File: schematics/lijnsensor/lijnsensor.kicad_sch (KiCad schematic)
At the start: 29 parts, among them J1 Conn_01x04_Pin, U10 AS7343xDLG, U11 AS7343xDLG, U2 TCA9548APWR, U3 TLV75718PDBV, U4 AS7343xDLG, U5 AS7343xDLG, U6 AS7343xDLG, U7 AS7343xDLG, U8 AS7343xDLG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

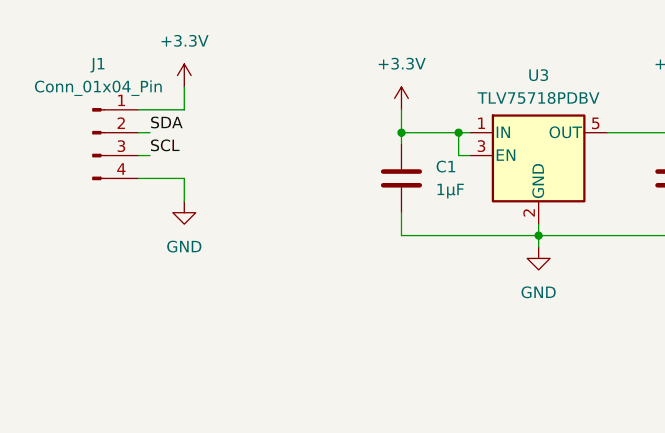
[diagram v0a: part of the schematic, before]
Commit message: ESD bescherming voor de lijnsensor
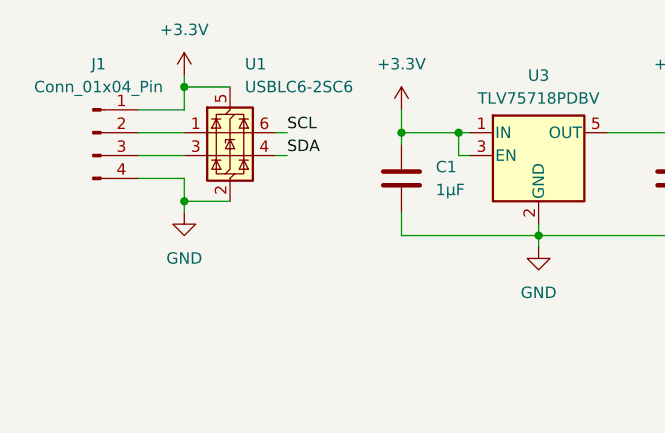
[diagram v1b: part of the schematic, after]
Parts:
- added U1: USBLC6-2SC6, Package_TO_SOT_SMD:SOT-23-6, symbol Power_Protection:USBLC6-2SC6
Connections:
- net +3.3V: now also U1.5 (VBUS)
- net GND: now also U1.2 (GND)
- net SCL: now also U1.6 (I/O1); no longer J1.3 (Pin_3)
- net SDA: now also U1.4 (I/O2); no longer J1.2 (Pin_2)
- new net: J1.2 (Pin_2), U1.1 (I/O1)
- new net: J1.3 (Pin_3), U1.3 (I/O2)
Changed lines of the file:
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@@
 	)
 	(junction
+		(at 33.02 21.59)
+		(diameter 0)
+		(color 255 0 0 1)
+	)
+	(junction
 		(at 78.74 160.02)
 		(diameter 0)
@@
 	)
 	(junction
+		(at 33.02 34.29)
+		(diameter 0)
+		(color 0 0 0 1)
+	)
+	(junction
 		(at 149.86 83.82)
 		(diameter 0)
@@
 	(wire
 		(pts
+			(xy 27.94 29.21) (xy 33.02 29.21)
+		)
+		(stroke
+			(width 0)
+			(type default)
+		)
+	)
+	(wire
+		(pts
 			(xy 147.32 151.13) (xy 147.32 154.94)
 		)
@@
 	(wire
 		(pts
+			(xy 33.02 21.59) (xy 38.1 21.59)
+		)
+		(stroke
+			(width 0)
+			(type default)
+			(color 255 0 0 1)
+		)
+	)
+	(wire
+		(pts
 			(xy 125.73 158.75) (xy 125.73 160.02)
 		)
@@
 	(wire
 		(pts
+			(xy 43.18 26.67) (xy 44.45 26.67)
+		)
+		(stroke
+			(width 0)
+			(type default)
+		)
+	)
+	(wire
+		(pts
 			(xy 72.39 36.83) (xy 72.39 38.1)
 		)
@@
 	(wire
 		(pts
-			(xy 27.94 26.67) (xy 29.21 26.67)
-		)
-		(stroke
-			(width 0)
-			(type default)
-		)
-	)
-	(wire
-		(pts
 			(xy 106.68 31.75) (xy 133.35 31.75)
 		)
@@
 	(wire
 		(pts
-			(xy 27.94 29.21) (xy 29.21 29.21)
+			(xy 114.3 147.32) (xy 100.33 147.32)
 		)
 		(stroke
@@
 	(wire
 		(pts
-			(xy 114.3 147.32) (xy 100.33 147.32)
+			(xy 100.33 144.78) (xy 113.03 144.78)
 		)
 		(stroke
@@
 	(wire
 		(pts
-			(xy 100.33 144.78) (xy 113.03 144.78)
+			(xy 125.73 72.39) (xy 125.73 73.66)
 		)
 		(stroke
@@
 	(wire
 		(pts
-			(xy 125.73 72.39) (xy 125.73 73.66)
+			(xy 109.22 170.18) (xy 100.33 170.18)
 		)
 		(stroke
@@
 	(wire
 		(pts
-			(xy 109.22 170.18) (xy 100.33 170.18)
+			(xy 33.02 34.29) (xy 33.02 35.56)
 		)
 		(stroke
 			(width 0)
 			(type default)
+			(color 0 0 0 1)
 		)
 	)
@@
 	(wire
 		(pts
+			(xy 33.02 21.59) (xy 33.02 24.13)
+		)
+		(stroke
+			(width 0)
+			(type default)
+			(color 255 0 0 1)
+		)
+	)
+	(wire
+		(pts
 			(xy 100.33 162.56) (xy 133.35 162.56)
 		)
@@
 	(wire
 		(pts
+			(xy 27.94 26.67) (xy 33.02 26.67)
+		)
+		(stroke
+			(width 0)
+			(type default)
+		)
+	)
+	(wire
+		(pts
 			(xy 125.73 95.25) (xy 115.57 95.25)
 		)
@@
 	(wire
 		(pts
+			(xy 43.18 29.21) (xy 44.45 29.21)
+		)
+		(stroke
+			(width 0)
+			(type default)
+		)
+	)
+	(wire
+		(pts
 			(xy 121.92 160.02) (xy 121.92 165.1)
 		)
@@
 	(wire
 		(pts
-			(xy 33.02 21.59) (xy 33.02 24.13)
+			(xy 33.02 20.32) (xy 33.02 21.59)
 		)
 		(stroke
@@
 	(wire
 		(pts
+			(xy 33.02 34.29) (xy 38.1 34.29)
+		)
+		(stroke
+			(width 0)
+			(type default)
+			(color 0 0 0 1)
+		)
+	)
+	(wire
+		(pts
 			(xy 125.73 73.66) (xy 137.16 73.66)
 		)
@@
 	)
 	(label "SDA"
-		(at 29.21 26.67 0)
+		(at 44.45 29.21 0)
 		(effects
 			(font
@@
 	)
 	(label "SCL"
-		(at 29.21 29.21 0)
+		(at 44.45 26.67 0)
 		(effects
 			(font
@@
 	(symbol
 		(lib_id "power:+3.3V")
-		(at 33.02 21.59 0)
+		(at 33.02 20.32 0)
 		(unit 1)
 		(exclude_from_sim no)
@@
 		(fields_autoplaced yes)
 		(property "Reference" "#PWR06"
-			(at 33.02 25.4 0)
+			(at 33.02 24.13 0)
 			(effects
 				(font
@@
 		)
 		(property "Value" "+3.3V"
-			(at 33.02 16.51 0)
+			(at 33.02 15.24 0)
 			(effects
 				(font
@@
 		)
 		(property "Footprint" ""
-			(at 33.02 21.59 0)
+			(at 33.02 20.32 0)
 			(effects
 				(font
@@
 		)
 		(property "Datasheet" ""
-			(at 33.02 21.59 0)
+			(at 33.02 20.32 0)
 			(effects
 				(font
@@
 		)
 		(property "Description" "Power symbol creates a global label with name \"+3.3V\""
-			(at 33.02 21.59 0)
+			(at 33.02 20.32 0)
 			(effects
 				(font
@@
 	(symbol
 		(lib_id "power:GND")
-		(at 33.02 34.29 0)
+		(at 33.02 35.56 0)
 		(unit 1)
 		(exclude_from_sim no)
@@
 		(fields_autoplaced yes)
 		(property "Reference" "#PWR01"
-			(at 33.02 40.64 0)
+			(at 33.02 41.91 0)
 			(effects
 				(font
@@
 		)
 		(property "Value" "GND"
-			(at 33.02 39.37 0)
+			(at 33.02 40.64 0)
 			(effects
 				(font
@@
 		)
 		(property "Footprint" ""
-			(at 33.02 34.29 0)
+			(at 33.02 35.56 0)
 			(effects
 				(font
@@
 		)
 		(property "Datasheet" ""
-			(at 33.02 34.29 0)
+			(at 33.02 35.56 0)
 			(effects
 				(font
@@
 		)
 		(property "Description" "Power symbol creates a global label with name \"GND\" , ground"
-			(at 33.02 34.29 0)
+			(at 33.02 35.56 0)
 			(effects
 				(font
@@
 		(on_board yes)
 		(dnp no)
-		(fields_autoplaced yes)
 		(property "Reference" "J1"
 			(at 23.495 19.05 0)
@@
 					(unit 1)
 				)
+			)
+		)
+	)
+	(symbol
+		(lib_id "Power_Protection:USBLC6-2SC6")
+		(at 38.1 26.67 0)
+		(unit 1)
+		(exclude_from_sim no)
+		(in_bom yes)
+		(on_board yes)
+		(dnp no)
+		(fields_autoplaced yes)
+		(property "Reference" "U1"
+			(at 39.7511 19.05 0)
+			(effects
+				(font
+					(size 1.27 1.27)
+				)
+				(justify left)
+			)
+		)
+		(property "Value" "USBLC6-2SC6"
+			(at 39.7511 21.59 0)
+			(effects
+				(font
+					(size 1.27 1.27)
+				)
+				(justify left)
+			)
+		)
+		(property "Footprint" "Package_TO_SOT_SMD:SOT-23-6"
+			(at 39.37 33.02 0)
+			(effects
+				(font
+					(size 1.27 1.27)
+					(italic yes)
+				)
+				(justify left)
+				(hide yes)
+			)
+		)
+		(property "Datasheet" "https://www.st.com/resource/en/datasheet/usblc6-2.pdf"
+			(at 39.37 34.925 0)
+			(effects
+				(font
+					(size 1.27 1.27)
+				)
+				(justify left)
+				(hide yes)
+			)
+		)
+		(property "Description" "Very low capacitance ESD protection diode, 2 data-line, SOT-23-6"
+			(at 38.1 26.67 0)
+			(effects
+				(font
+					(size 1.27 1.27)
+				)
+				(hide yes)
+			)
+		)
+		(pin "5"
+		)
+		(pin "3"
+		)
+		(pin "4"
+		)
+		(pin "2"
+		)
+		(pin "6"
+		)
+		(pin "1"
+		)
+		(instances
+			(project ""
+				(path "/a6ffd0d1-4626-482d-83b6-201a497e75b4"
+					(reference "U1")
+					(unit 1)
+				)

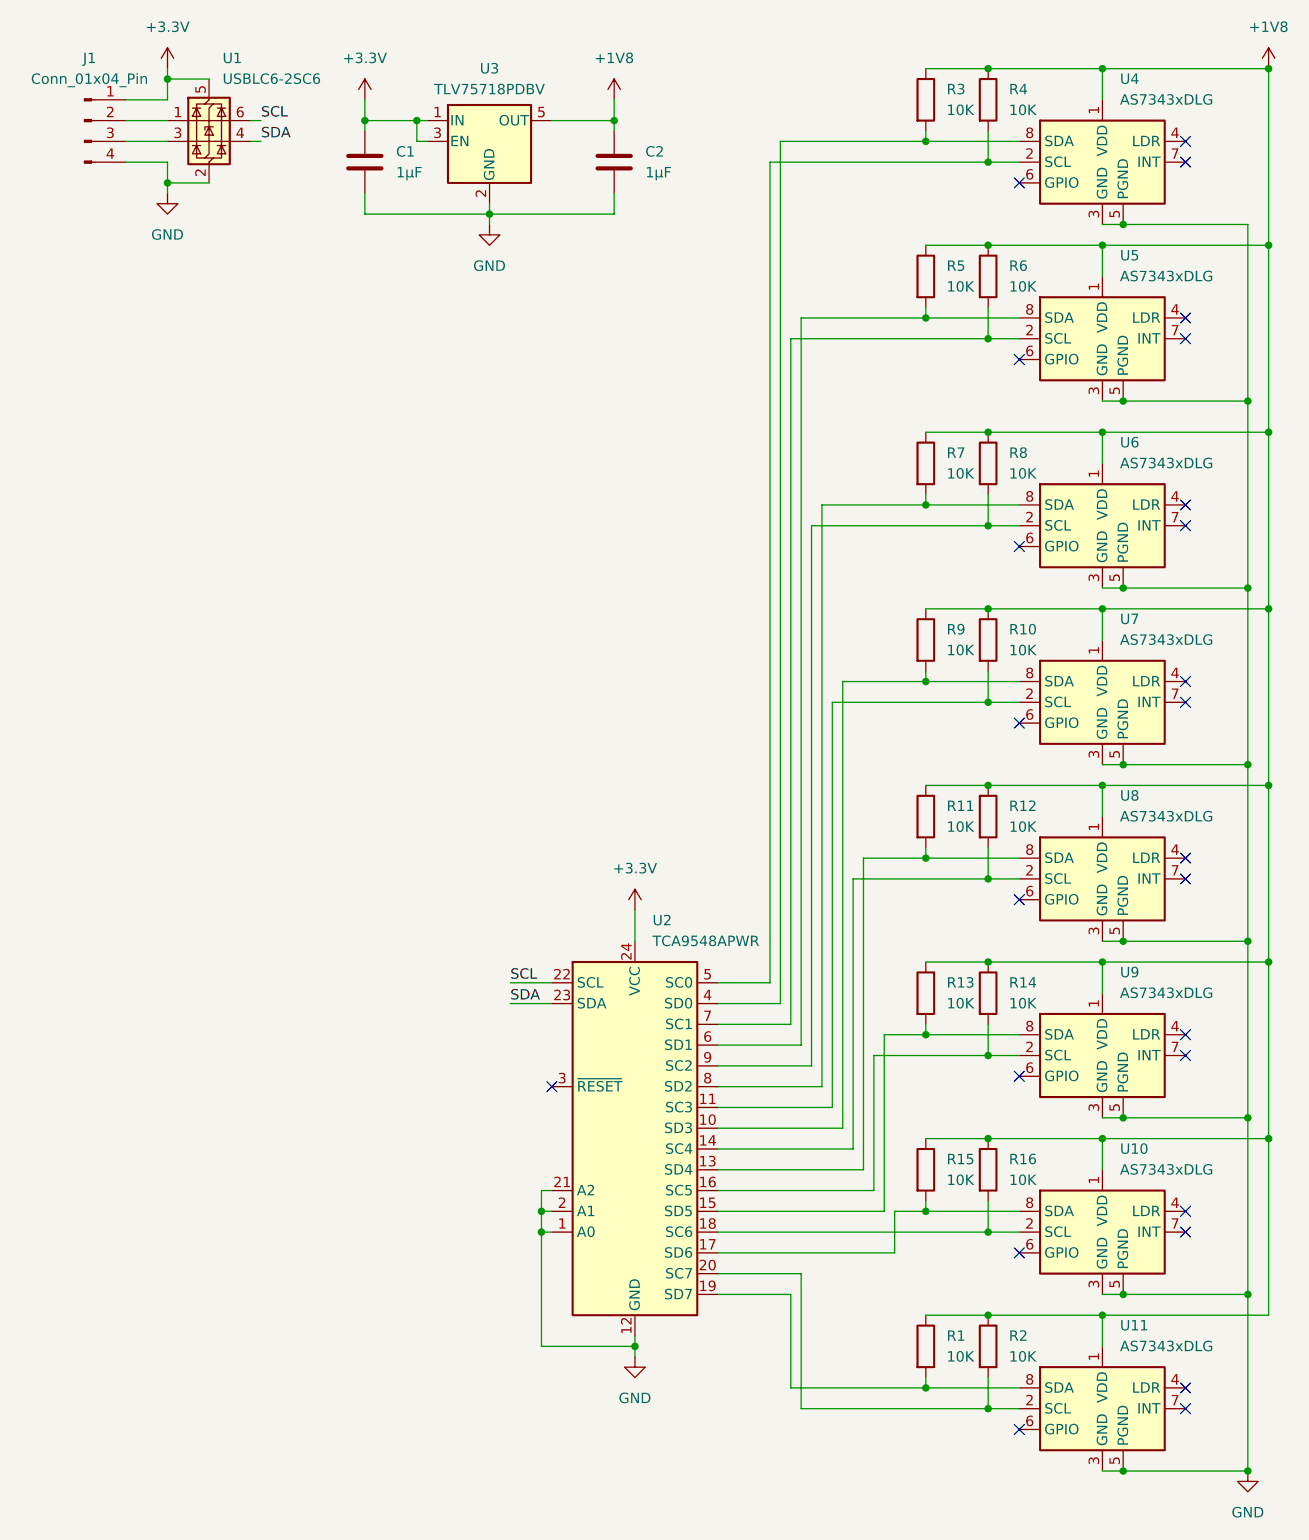
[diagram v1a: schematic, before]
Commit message: de routing is klaar van de lijnsensor nog allen opschonen
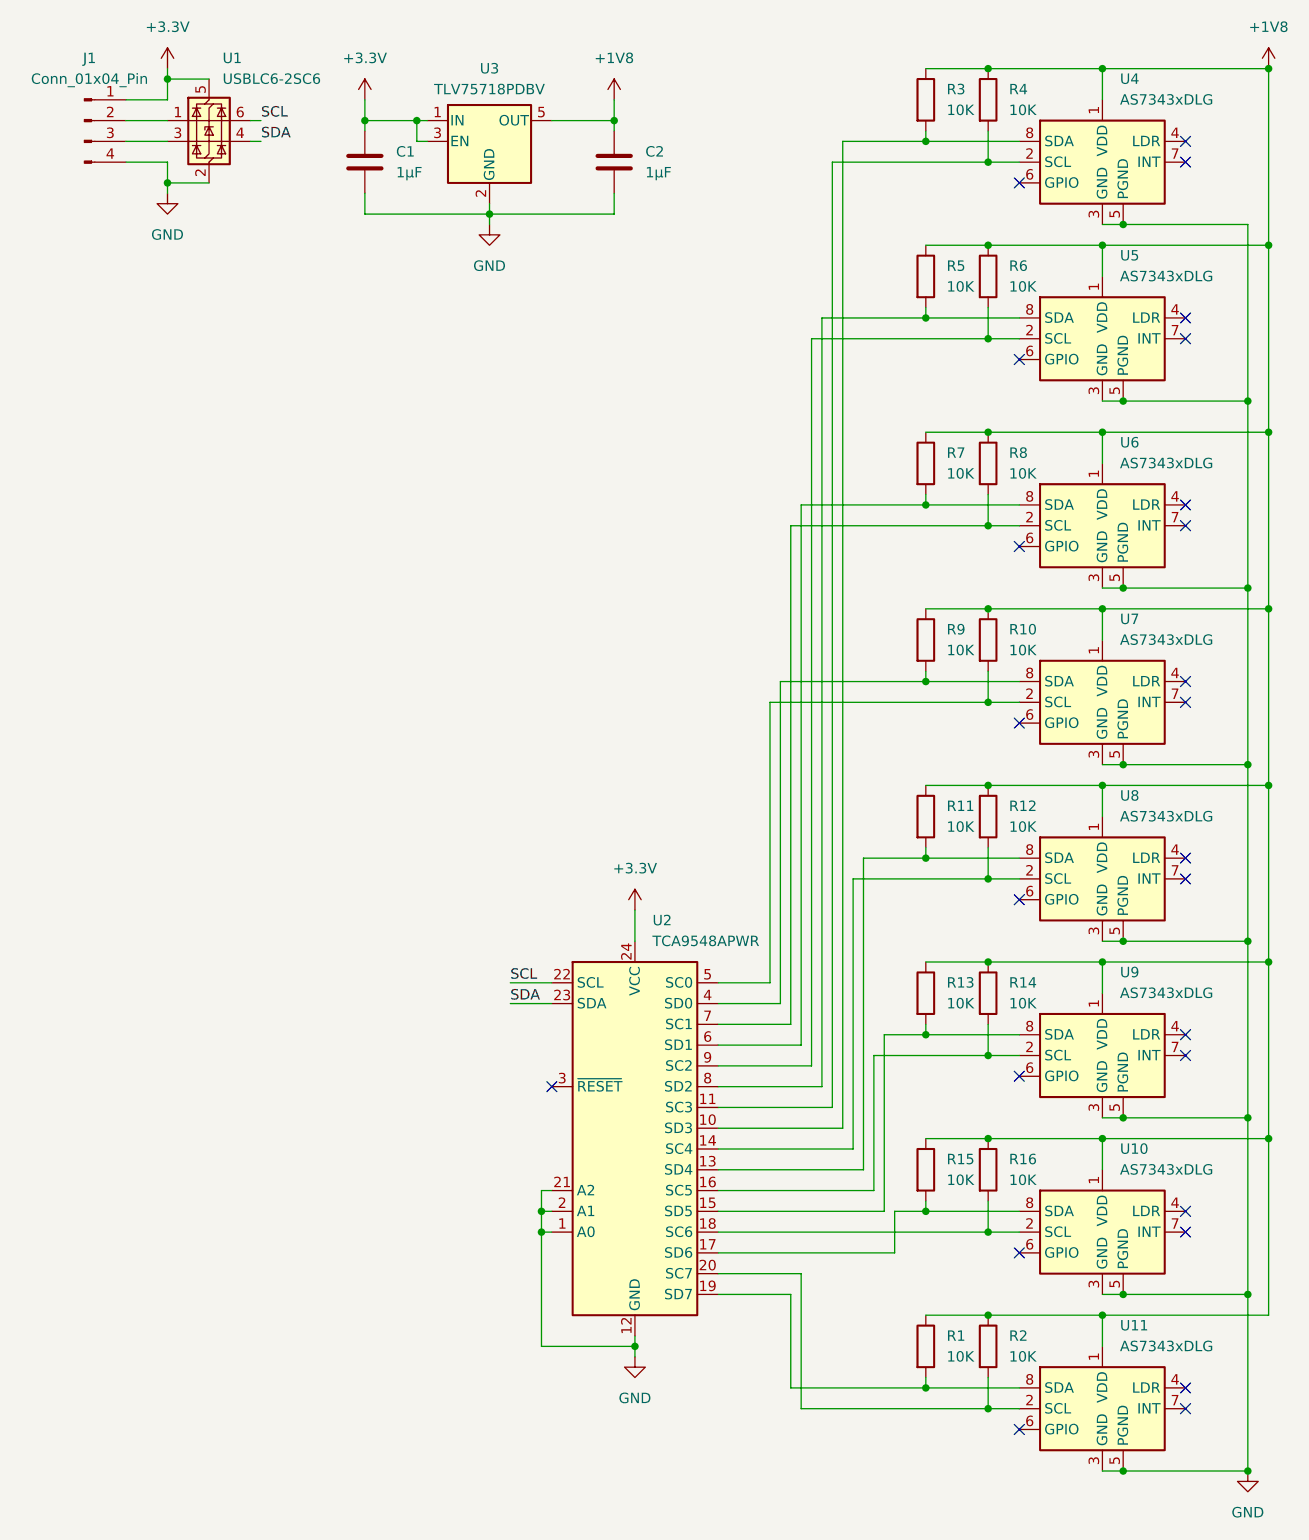
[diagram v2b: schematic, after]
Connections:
- net at R9.2, U7.8 (SDA): now also U2.4 (SD0); no longer U2.10 (SD3)
- net at R10.2, U7.2 (SCL): now also U2.5 (SC0); no longer U2.11 (SC3)
- net at R3.2, U4.8 (SDA): now also U2.10 (SD3); no longer U2.4 (SD0)
- net at R4.2, U4.2 (SCL): now also U2.11 (SC3); no longer U2.5 (SC0)
- net at R5.2, U5.8 (SDA): now also U2.8 (SD2); no longer U2.6 (SD1)
- net at R6.2, U5.2 (SCL): now also U2.9 (SC2); no longer U2.7 (SC1)
- net at R7.2, U6.8 (SDA): now also U2.6 (SD1); no longer U2.8 (SD2)
- net at R8.2, U6.2 (SCL): now also U2.7 (SC1); no longer U2.9 (SC2)
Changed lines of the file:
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@@
+	(wire
+		(pts
+			(xy 110.49 139.7) (xy 110.49 73.66)
+		)
+		(stroke
+			(width 0)
+			(type default)
+		)
+	)
 	(wire
 		(pts
@@
 	(wire
 		(pts
+			(xy 114.3 31.75) (xy 133.35 31.75)
+		)
+		(stroke
+			(width 0)
+			(type default)
+		)
+	)
+	(wire
+		(pts
 			(xy 119.38 157.48) (xy 100.33 157.48)
 		)
@@
 	(wire
 		(pts
-			(xy 115.57 95.25) (xy 115.57 149.86)
-		)
-		(stroke
-			(width 0)
-			(type default)
-		)
-	)
-	(wire
-		(pts
 			(xy 64.77 29.21) (xy 63.5 29.21)
 		)
@@
 	(wire
 		(pts
-			(xy 106.68 31.75) (xy 106.68 132.08)
-		)
-		(stroke
-			(width 0)
-			(type default)
-		)
-	)
-	(wire
-		(pts
 			(xy 133.35 27.94) (xy 133.35 31.75)
 		)
@@
 	(wire
 		(pts
-			(xy 113.03 73.66) (xy 125.73 73.66)
-		)
-		(stroke
-			(width 0)
-			(type default)
-		)
-	)
-	(wire
-		(pts
 			(xy 125.73 180.34) (xy 125.73 181.61)
 		)
@@
 	(wire
 		(pts
+			(xy 107.95 95.25) (xy 125.73 95.25)
+		)
+		(stroke
+			(width 0)
+			(type default)
+		)
+	)
+	(wire
+		(pts
 			(xy 147.32 41.91) (xy 167.64 41.91)
 		)
@@
 	(wire
 		(pts
+			(xy 114.3 147.32) (xy 114.3 31.75)
+		)
+		(stroke
+			(width 0)
+			(type default)
+		)
+	)
+	(wire
+		(pts
 			(xy 74.93 132.08) (xy 80.01 132.08)
 		)
@@
 	(wire
 		(pts
-			(xy 111.76 76.2) (xy 111.76 142.24)
-		)
-		(stroke
-			(width 0)
-			(type default)
-		)
-	)
-	(wire
-		(pts
-			(xy 106.68 31.75) (xy 133.35 31.75)
-		)
-		(stroke
-			(width 0)
-			(type default)
-		)
-	)
-	(wire
-		(pts
 			(xy 165.1 60.96) (xy 165.1 83.82)
 		)
@@
 	(wire
 		(pts
-			(xy 109.22 53.34) (xy 109.22 137.16)
-		)
-		(stroke
-			(width 0)
-			(type default)
-		)
-	)
-	(wire
-		(pts
-			(xy 107.95 29.21) (xy 107.95 134.62)
-		)
-		(stroke
-			(width 0)
-			(type default)
-		)
-	)
-	(wire
-		(pts
 			(xy 100.33 132.08) (xy 106.68 132.08)
 		)
@@
 	(wire
 		(pts
+			(xy 113.03 50.8) (xy 113.03 144.78)
+		)
+		(stroke
+			(width 0)
+			(type default)
+		)
+	)
+	(wire
+		(pts
 			(xy 125.73 20.32) (xy 133.35 20.32)
 		)
@@
 	(wire
 		(pts
+			(xy 109.22 76.2) (xy 133.35 76.2)
+		)
+		(stroke
+			(width 0)
+			(type default)
+		)
+	)
+	(wire
+		(pts
 			(xy 72.39 38.1) (xy 87.63 38.1)
 		)
@@
 	(wire
 		(pts
-			(xy 110.49 50.8) (xy 125.73 50.8)
+			(xy 106.68 132.08) (xy 106.68 97.79)
 		)
 		(stroke
@@
 	(wire
 		(pts
-			(xy 113.03 144.78) (xy 113.03 73.66)
-		)
-		(stroke
-			(width 0)
-			(type default)
-		)
-	)
-	(wire
-		(pts
 			(xy 137.16 140.97) (xy 133.35 140.97)
 		)
@@
 	(wire
 		(pts
-			(xy 133.35 97.79) (xy 114.3 97.79)
-		)
-		(stroke
-			(width 0)
-			(type default)
-		)
-	)
-	(wire
-		(pts
 			(xy 133.35 129.54) (xy 147.32 129.54)
 		)
@@
 	(wire
 		(pts
-			(xy 133.35 76.2) (xy 111.76 76.2)
-		)
-		(stroke
-			(width 0)
-			(type default)
-		)
-	)
-	(wire
-		(pts
 			(xy 149.86 105.41) (xy 165.1 105.41)
 		)
@@
 	(wire
 		(pts
-			(xy 110.49 139.7) (xy 110.49 50.8)
-		)
-		(stroke
-			(width 0)
-			(type default)
-		)
-	)
-	(wire
-		(pts
 			(xy 165.1 148.59) (xy 165.1 170.18)
 		)
@@
 	(wire
 		(pts
+			(xy 109.22 137.16) (xy 109.22 76.2)
+		)
+		(stroke
+			(width 0)
+			(type default)
+		)
+	)
+	(wire
+		(pts
+			(xy 113.03 50.8) (xy 125.73 50.8)
+		)
+		(stroke
+			(width 0)
+			(type default)
+		)
+	)
+	(wire
+		(pts
 			(xy 149.86 148.59) (xy 165.1 148.59)
 		)
@@
 	(wire
 		(pts
+			(xy 111.76 53.34) (xy 133.35 53.34)
+		)
+		(stroke
+			(width 0)
+			(type default)
+		)
+	)
+	(wire
+		(pts
 			(xy 90.17 176.53) (xy 78.74 176.53)
 		)
@@
 	(wire
 		(pts
-			(xy 114.3 97.79) (xy 114.3 147.32)
+			(xy 110.49 73.66) (xy 125.73 73.66)
 		)
 		(stroke
@@
 	(wire
 		(pts
-			(xy 125.73 95.25) (xy 115.57 95.25)
-		)
-		(stroke
-			(width 0)
-			(type default)
-		)
-	)
-	(wire
-		(pts
 			(xy 147.32 90.17) (xy 147.32 86.36)
 		)
@@
 	(wire
 		(pts
-			(xy 107.95 29.21) (xy 125.73 29.21)
+			(xy 115.57 29.21) (xy 115.57 149.86)
+		)
+		(stroke
+			(width 0)
+			(type default)
+		)
+	)
+	(wire
+		(pts
+			(xy 115.57 29.21) (xy 125.73 29.21)
 		)
 		(stroke
@@
 	(wire
 		(pts
+			(xy 111.76 142.24) (xy 111.76 53.34)
+		)
+		(stroke
+			(width 0)
+			(type default)
+		)
+	)
+	(wire
+		(pts
 			(xy 167.64 107.95) (xy 147.32 107.95)
 		)
@@
 	(wire
 		(pts
-			(xy 133.35 53.34) (xy 109.22 53.34)
-		)
-		(stroke
-			(width 0)
-			(type default)
-		)
-	)
-	(wire
-		(pts
 			(xy 33.02 34.29) (xy 38.1 34.29)
 		)
@@
 	(wire
 		(pts
+			(xy 107.95 95.25) (xy 107.95 134.62)
+		)
+		(stroke
+			(width 0)
+			(type default)
+		)
+	)
+	(wire
+		(pts
 			(xy 125.73 129.54) (xy 133.35 129.54)
 		)
@@
 		)
 	)
+	(wire
+		(pts
+			(xy 106.68 97.79) (xy 133.35 97.79)
+		)
+		(stroke
+			(width 0)
+			(type default)
+		)
+	)
